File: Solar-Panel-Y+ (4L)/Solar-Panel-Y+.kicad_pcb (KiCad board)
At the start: 4 copper layers, 50 x 50 mm, 81 parts, among them J1 FTS-105-01-L-DV-A, Q1 BSS138DWQ-7, Q2 MBT2222ADW1T1, Q3 BSS138DWQ-7, Q4 MBT2222ADW1T1, U1 Value, U2 TSL2561

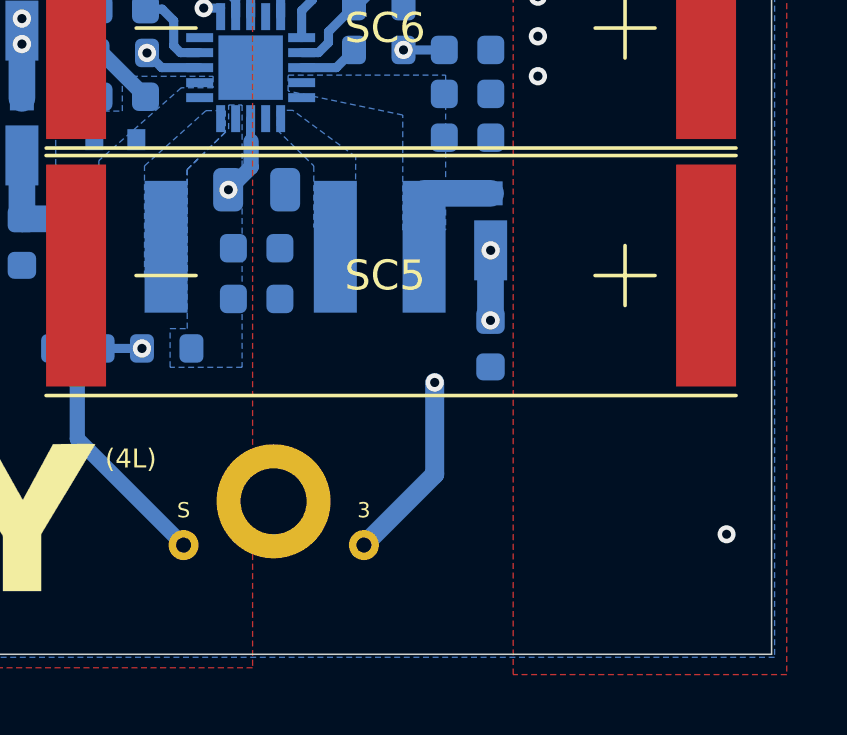
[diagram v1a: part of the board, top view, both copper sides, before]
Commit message: Fix Rail Interference issues
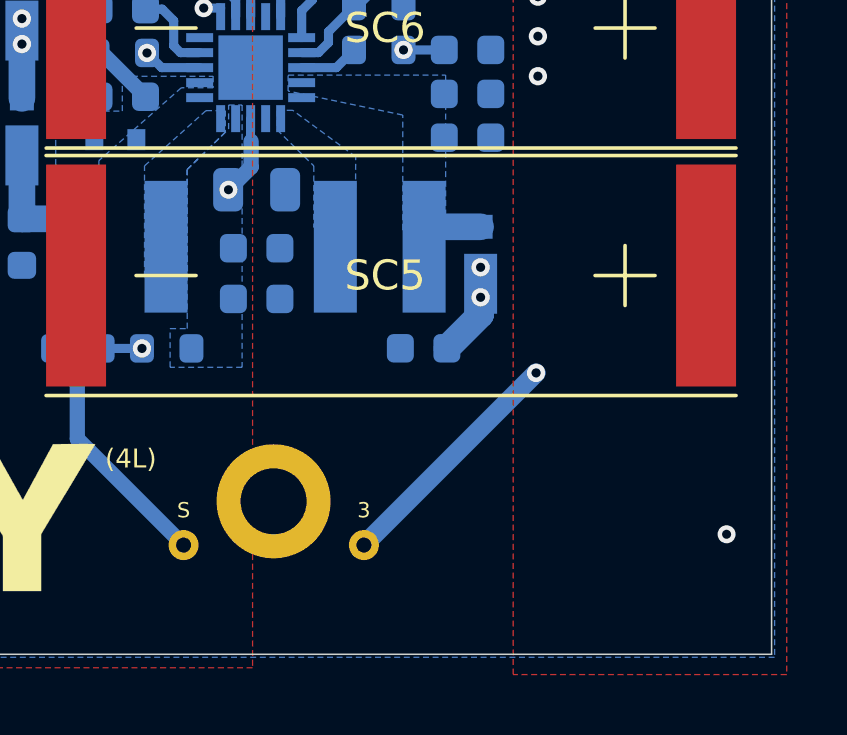
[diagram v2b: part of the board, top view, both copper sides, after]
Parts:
- moved C11 2.24 mm to (118.0, 75.0), turned to 180 degrees
- moved D2 1.16 mm to (119.9, 72.2)
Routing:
- net +3V3: track 18.3 -> 19.9 mm
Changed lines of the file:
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@@
   )
   (footprint "Capacitor_SMD:C_0603_1608Metric" (layer "B.Cu")
-    (at 120.23 74.845 -90)
+    (at 118 75 180)
     (descr "Capacitor SMD 0603 (1608 Metric), square (rectangular) end terminal, IPC_7351 nominal, (Body size source: IPC-SM-782 page 76, https://www.pcb-3d.com/wordpress/wp-content/uploads/ipc-sm-782a_amendment_1_and_2.pdf), generated with kicad-footprint-generator")
     (tags "capacitor")
@@
     (property "Sheetname" "")
     (attr smd)
-    (fp_text reference "C11" (at 1.01 1.55) (layer "B.SilkS")
+    (fp_text reference "C11" (at 2.4 0 180) (layer "B.SilkS")
       (effects (font (size 0.508 0.508) (thickness 0.1016)) (justify mirror))
     )
-    (fp_text value "0.1uF" (at 0 -1.43 90) (layer "B.Fab")
+    (fp_text value "0.1uF" (at 0 -1.43) (layer "B.Fab")
       (effects (font (size 1 1) (thickness 0.15)) (justify mirror))
     )
-    (fp_text user "${REFERENCE}" (at 0 0 90) (layer "B.Fab")
+    (fp_text user "${REFERENCE}" (at 0 0) (layer "B.Fab")
       (effects (font (size 0.4 0.4) (thickness 0.06)) (justify mirror))
     )
@@
     (fp_line (start -0.8 0.4) (end 0.8 0.4) (layer "B.Fab") (width 0.1))
     (fp_line (start -0.8 -0.4) (end -0.8 0.4) (layer "B.Fab") (width 0.1))
-    (pad "1" smd roundrect (at -0.775 0 270) (size 0.9 0.95) (layers "B.Cu" "B.Paste" "B.Mask") (roundrect_rratio 0.25)
+    (pad "1" smd roundrect (at -0.775 0 180) (size 0.9 0.95) (layers "B.Cu" "B.Paste" "B.Mask") (roundrect_rratio 0.25)
       (net 5 "+3V3") (pintype "passive"))
-    (pad "2" smd roundrect (at 0.775 0 270) (size 0.9 0.95) (layers "B.Cu" "B.Paste" "B.Mask") (roundrect_rratio 0.25)
+    (pad "2" smd roundrect (at 0.775 0 180) (size 0.9 0.95) (layers "B.Cu" "B.Paste" "B.Mask") (roundrect_rratio 0.25)
       (net 4 "GND") (pintype "passive"))
     (model "${KICAD6_3DMODEL_DIR}/Capacitor_SMD.3dshapes/C_0603_1608Metric.step"
@@
   )
   (footprint "solarpanels:MICROSMP" (layer "B.Cu")
-    (at 120.235 71.085 90)
+    (at 119.9 72.2 90)
     (descr "MicroSMP")
     (tags "Schottky Diode")
@@
   (gr_line (start 103.313916 48.22) (end 103.631416 48.22) (layer "B.SilkS") (width 0.12))
   (gr_line (start 104.38 48.22) (end 104.0625 48.22) (layer "B.SilkS") (width 0.12))
-  (gr_line (start 121 43.8) (end 121 36.8) (layer "B.SilkS") (width 0.0254))
-  (gr_line (start 121 53.59) (end 121 76.6) (layer "B.SilkS") (width 0.0254))
-  (gr_line (start 121 43.8) (end 121 48.57) (layer "B.SilkS") (width 0.0254))
-  (gr_line (start 121 76.6) (end 121 83.6) (layer "B.SilkS") (width 0.0254))
+  (gr_line (start 121 53.59) (end 121 73.6) (layer "B.SilkS") (width 0.0254))
+  (gr_line (start 121 46.8) (end 121 48.57) (layer "B.SilkS") (width 0.0254))
   (gr_line (start 105.86 48.22) (end 105.5425 48.22) (layer "B.SilkS") (width 0.12))
-  (gr_line (start 88.2 76.6) (end 88.2 83.6) (layer "B.SilkS") (width 0.0254))
-  (gr_line (start 128 76.6) (end 121 76.6) (layer "B.SilkS") (width 0.0254))
-  (gr_line (start 88.2 43.8) (end 88.2 76.6) (layer "B.SilkS") (width 0.0254))
-  (gr_line (start 81.2 76.6) (end 88.2 76.6) (layer "B.SilkS") (width 0.0254))
+  (gr_line (start 88.2 46.8) (end 88.2 73.6) (layer "B.SilkS") (width 0.0254))
+  (gr_arc (start 88.2 46.8) (mid 89.07868 44.67868) (end 91.2 43.8) (layer "B.SilkS") (width 0.0254))
+  (gr_arc (start 121 73.6) (mid 120.12132 75.72132) (end 118 76.6) (layer "B.SilkS") (width 0.0254))
   (gr_line (start 88.2 36.8) (end 81.2 36.8) (layer "B.SilkS") (width 0.0254))
   (gr_line (start 88.2 83.6) (end 81.2 83.6) (layer "B.SilkS") (width 0.0254))
@@
   (gr_line (start 104.793916 48.22) (end 105.111416 48.22) (layer "B.SilkS") (width 0.12))
   (gr_line (start 128 35.24) (end 128 43.8) (layer "B.SilkS") (width 0.0254))
+  (gr_arc (start 91.2 76.6) (mid 89.07868 75.72132) (end 88.2 73.6) (layer "B.SilkS") (width 0.0254))
   (gr_line (start 128 85.16) (end 128 76.6) (layer "B.SilkS") (width 0.0254))
   (gr_line (start 79.64 83.6) (end 129.56 83.6) (layer "B.SilkS") (width 0.0254))
   (gr_line (start 128 43.8) (end 128 76.6) (layer "B.SilkS") (width 0.0254))
-  (gr_line (start 128 43.8) (end 121 43.8) (layer "B.SilkS") (width 0.0254))
   (gr_line (start 121 36.8) (end 128 36.8) (layer "B.SilkS") (width 0.0254))
   (gr_line (start 81.2 83.6) (end 81.2 76.6) (layer "B.SilkS") (width 0.0254))
-  (gr_line (start 81.21 43.8) (end 88.21 43.8) (layer "B.SilkS") (width 0.0254))
+  (gr_arc (start 118 43.8) (mid 120.12132 44.67868) (end 121 46.8) (layer "B.SilkS") (width 0.0254))
   (gr_rect (start 119.07 53.585) (end 127.28 48.615) (layer "B.SilkS") (width 0.12) (fill none))
-  (gr_line (start 88.2 43.8) (end 88.2 36.8) (layer "B.SilkS") (width 0.0254))
   (gr_line (start 81.2 35.24) (end 81.2 85.16) (layer "B.SilkS") (width 0.0254))
-  (gr_line (start 88.2 76.6) (end 121 76.6) (layer "B.SilkS") (width 0.0254))
+  (gr_line (start 91.2 76.6) (end 118 76.6) (layer "B.SilkS") (width 0.0254))
   (gr_line (start 121 83.6) (end 128 83.6) (layer "B.SilkS") (width 0.0254))
-  (gr_line (start 121 43.8) (end 88.2 43.8) (layer "B.SilkS") (width 0.0254))
+  (gr_line (start 118 43.8) (end 91.2 43.8) (layer "B.SilkS") (width 0.0254))
   (gr_circle (center 104.61 50.04) (end 104.991 50.04) (layer "F.Mask") (width 0) (fill solid))
   (gr_circle (center 104.61 46.41) (end 104.991 46.41) (layer "F.Mask") (width 0) (fill solid))
@@
   (segment (start 109.25 40.4) (end 106.21 40.4) (width 0.381) (layer "F.Cu") (net 5))
   (via (at 90.78 61.575) (size 0.6096) (drill 0.3048) (layers "F.Cu" "B.Cu") (net 5))
-  (via (at 118.37 76.14) (size 0.6096) (drill 0.3048) (layers "F.Cu" "B.Cu") (net 5))
   (via (at 90.79 49.495) (size 0.6096) (drill 0.3048) (layers "F.Cu" "B.Cu") (net 5))
   (via (at 109.85 44.47) (size 0.6096) (drill 0.3048) (layers "F.Cu" "B.Cu") (net 5))
-  (via (at 120.235 71.735) (size 0.6096) (drill 0.3048) (layers "F.Cu" "B.Cu") (net 5))
+  (via (at 121.75 75.82) (size 0.6096) (drill 0.3048) (layers "F.Cu" "B.Cu") (net 5))
+  (via (at 119.9 72.3) (size 0.6096) (drill 0.3048) (layers "F.Cu" "B.Cu") (net 5))
   (via (at 113 48.56) (size 0.6096) (drill 0.3048) (layers "F.Cu" "B.Cu") (net 5))
   (via (at 111.51 48.56) (size 0.6096) (drill 0.3048) (layers "F.Cu" "B.Cu") (net 5))
   (via (at 90.79 57.195) (size 0.6096) (drill 0.3048) (layers "F.Cu" "B.Cu") (net 5))
-  (via (at 120.23 74.07) (size 0.6096) (drill 0.3048) (layers "F.Cu" "B.Cu") (net 5))
+  (via (at 119.9 73.3) (size 0.6096) (drill 0.3048) (layers "F.Cu" "B.Cu") (net 5))
   (via (at 90.78 53.875) (size 0.6096) (drill 0.3048) (layers "F.Cu" "B.Cu") (net 5))
   (via (at 98.07 55.43) (size 0.6096) (drill 0.3048) (layers "F.Cu" "B.Cu") (net 5))
   (via (at 98.18 63.125) (size 0.6096) (drill 0.3048) (layers "F.Cu" "B.Cu") (net 5))
+  (segment (start 119.9 73.875) (end 118.775 75) (width 0.889) (layer "B.Cu") (net 5))
   (segment (start 98.065 55.425) (end 97.02 55.425) (width 0.381) (layer "B.Cu") (net 5))
-  (segment (start 120.23 74.07) (end 120.23 71.74) (width 0.889) (layer "B.Cu") (net 5))
-  (segment (start 118.37 79.2) (end 116.01 81.56) (width 0.635) (layer "B.Cu") (net 5))
   (segment (start 98.175 63.12) (end 97.02 63.12) (width 0.381) (layer "B.Cu") (net 5))
+  (segment (start 121.75 75.82) (end 116.01 81.56) (width 0.635) (layer "B.Cu") (net 5))
+  (segment (start 119.9 73.3) (end 119.9 73.875) (width 0.889) (layer "B.Cu") (net 5))
   (segment (start 98.18 63.125) (end 98.175 63.12) (width 0.381) (layer "B.Cu") (net 5))
-  (segment (start 118.37 76.14) (end 118.37 79.2) (width 0.635) (layer "B.Cu") (net 5))
   (segment (start 98.07 55.43) (end 98.065 55.425) (width 0.381) (layer "B.Cu") (net 5))
   (segment (start 106.4564 78.0164) (end 110 81.56) (width 0.508) (layer "B.Cu") (net 6))
@@
   (segment (start 109.67 64.08) (end 109.285 63.695) (width 0.3048) (layer "B.Cu") (net 16))
   (segment (start 110.535 65.145) (end 109.895 65.145) (width 0.3048) (layer "B.Cu") (net 16))
-  (segment (start 120.235 69.835) (end 118.01653 69.835) (width 0.889) (layer "B.Cu") (net 17))
+  (segment (start 119.9 70.95) (end 117.85 70.95) (width 0.889) (layer "B.Cu") (net 17))
   (segment (start 106.05 39.61) (end 107.77 39.61) (width 0.381) (layer "F.Cu") (net 19))
   (via (at 121.81 63.28) (size 0.6096) (drill 0.3048) (layers "F.Cu" "B.Cu") (net 20))
